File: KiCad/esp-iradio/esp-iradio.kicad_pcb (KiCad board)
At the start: 4 copper layers, 122 x 76 mm, 122 parts, among them J201 USB-C TYPE-C-31-M-12, J202 Li-Po cell (JST-PH), J3 Display HS20S010B CN1, J4 microSD push-push TF-01A, J5 Line out 3.5mm PJ-320D, J6 Speaker 4-8 Ohm, J7 Display CN2 (mechanical), J8 Line out RCA L/R AV-210-WR, Q201 MMBT3904, Q202 MMBT3904, Q203 DMG2305UX-7, SW1 EC11 with switch, SW201 RESET, SW202 BOOT, SW203 ON/OFF MSK12C02, U1 PCM5102APWR, U2 MAX98357AETE+T, U201 BQ24074RGTT, U202 USBLC6-2SC6, U203 CH340C, U204 DW01A, U205 FS8205A, U206 AP7361C-33Y5-13, U207 TPLP5907MFX-3.3, U3 ESP32-WROVER-IE-N16R8

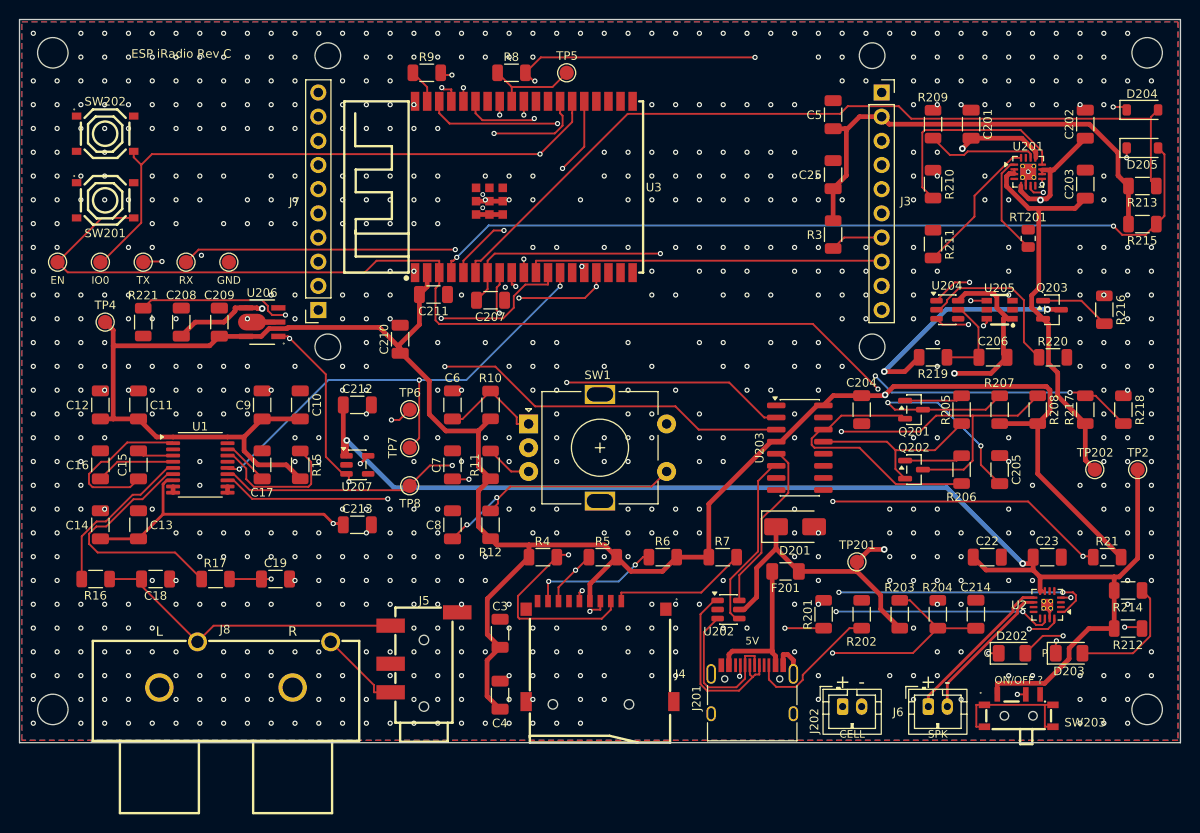
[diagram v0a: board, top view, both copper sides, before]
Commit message: USB-C flush with the bottom edge, cell connector on the right edge
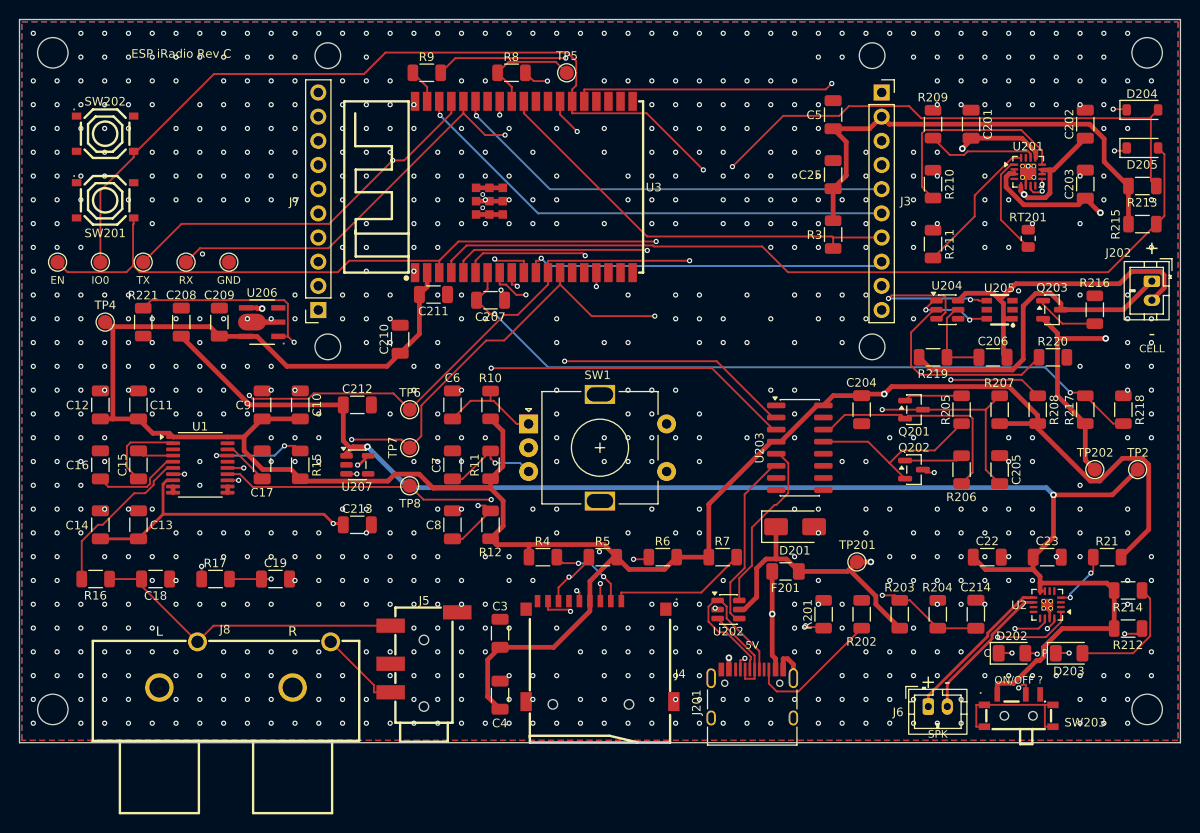
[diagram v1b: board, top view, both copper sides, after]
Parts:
- moved J202 55.3 mm to (219.0, 127.5), turned to -90 degrees
- moved R216 1.00 mm to (213.0, 130.5)
- moved J201 0.45 mm to (177.0, 172.3)
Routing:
- net Net-(J202-Pin_1): track 62.7 -> 33.9 mm, vias 2 -> 0
- net /Power, charger and USB/BATN: track 57.8 -> 34.1 mm, vias 1 -> 0
- net Net-(J4-DAT3/CD): track 78.6 -> 58.0 mm, vias 2 -> 3
- net +3V3: track 315.7 -> 330.5 mm
- net ESP_EN: track 138.1 -> 123.9 mm, vias 3 -> 2
- net Net-(C8-+): track 57.1 -> 71.2 mm, vias 3 -> 2
- net Net-(R17-+): track 25.8 -> 13.0 mm, vias 0 -> 2
- net Net-(R21-+): track 90.5 -> 103.0 mm, vias 4 -> 3
- net Net-(J3-Pin_4): track 115.2 -> 103.4 mm
- net Net-(U204-OC): track 7.91 -> 19.4 mm
- net Net-(U1-BCK): track 140.1 -> 128.7 mm
- net Net-(U1-DIN): track 127.1 -> 135.6 mm, vias 5 -> 3
- net /Power, charger and USB/VBAT: track 42.7 -> 50.8 mm, vias 0 -> 2
- net VBUS_SENSE: track 86.9 -> 78.8 mm
- net Net-(C15-+): track 17.0 -> 8.98 mm
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
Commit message: Speaker connector and switch moved left into the cell connector's old place
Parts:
- moved J6 9.00 mm to (186.5, 172.2)
- moved SW203 9.00 mm to (196.0, 172.6)
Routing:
- net Net-(J3-Pin_4): track 103.4 -> 119.9 mm
- net Net-(R21-+): track 103.0 -> 86.9 mm, vias 3 -> 2
- net Net-(C8-+): track 71.2 -> 56.5 mm, vias 2 -> 1
- net Net-(R17-+): track 13.0 -> 25.8 mm, vias 2 -> 0
- net Net-(U1-BCK): track 128.7 -> 119.1 mm
- net Net-(U204-OC): track 19.4 -> 9.81 mm, vias 2 -> 0
- net Net-(J4-DAT3/CD): track 58.0 -> 66.6 mm
- net Net-(J6-Pin_1): track 16.7 -> 25.1 mm, vias 0 -> 1
- net ESP_IO0: track 145.3 -> 137.3 mm
- net Net-(U1-DIN): track 135.6 -> 127.5 mm, vias 3 -> 4
- net Net-(C15-+): track 8.98 -> 17.0 mm
- net /Power, charger and USB/USB_D-: track 9.92 -> 17.5 mm, vias 0 -> 2
- net Net-(J6-Pin_2): track 15.3 -> 22.6 mm, vias 0 -> 1
- net /Power, charger and USB/EN_3V3: track 120.5 -> 127.1 mm
- net +3V3: track 330.5 -> 324.2 mm
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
